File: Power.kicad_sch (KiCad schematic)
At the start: 15 parts, among them J5 Conn_01x02, U1 TPS62840YBGR, U13 TPS62840YBGR, U7 LTC2941IDCB-1#TRMPBF

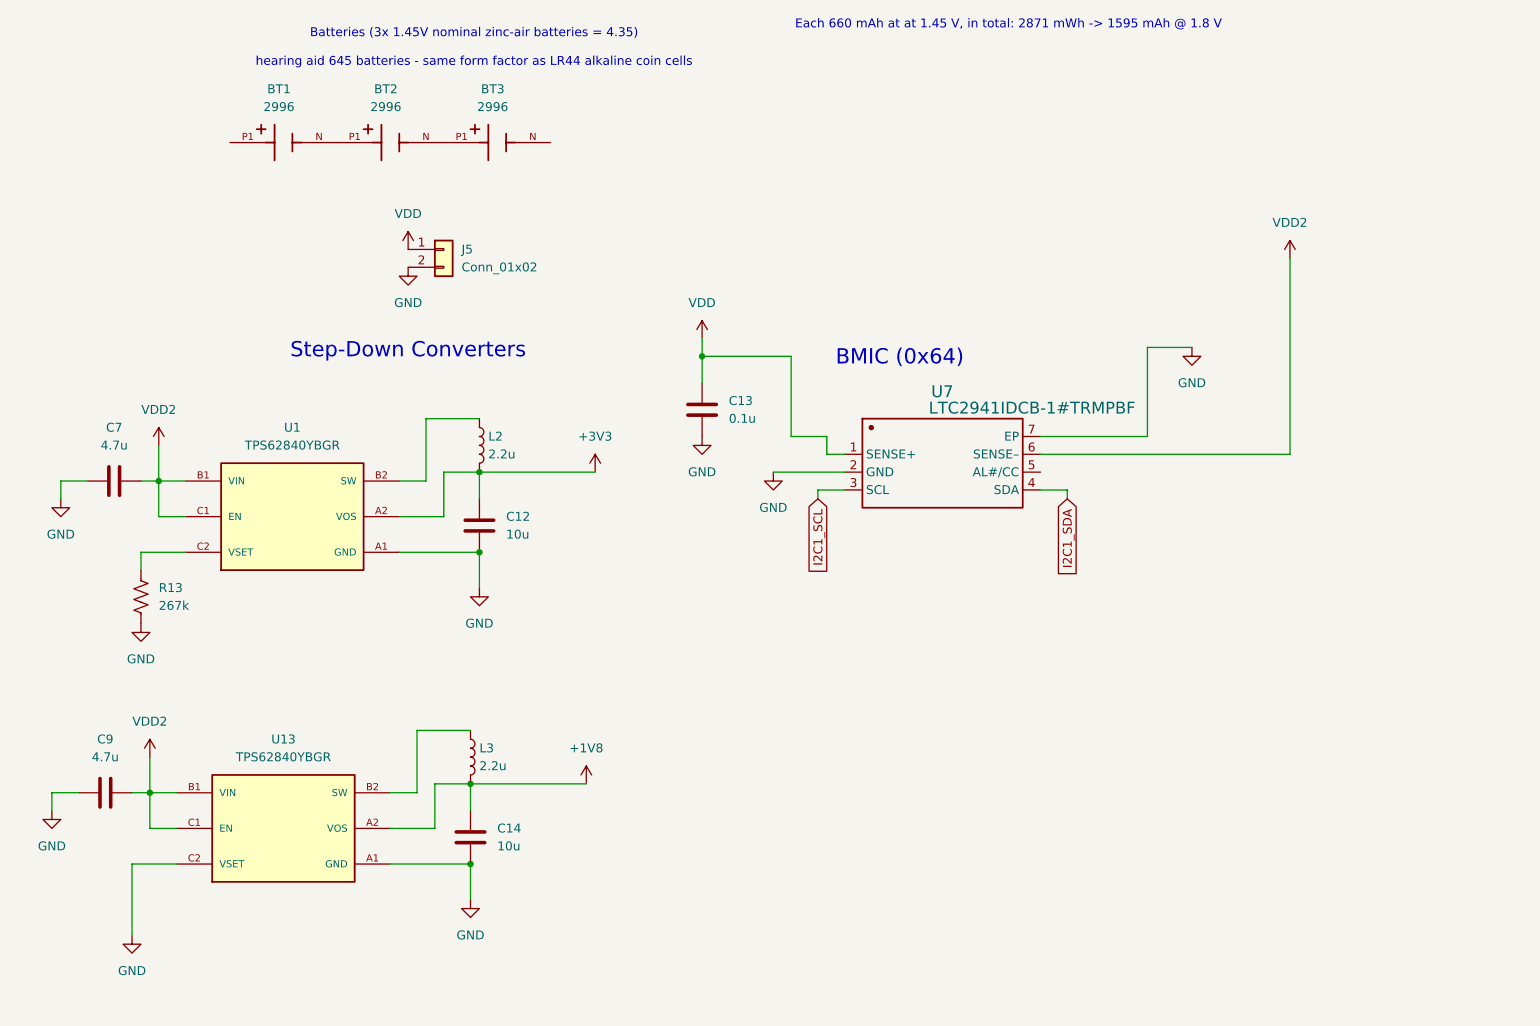
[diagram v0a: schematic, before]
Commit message: Add V2: STM32U575 LQFP-64 tag board and ST-Link dongle
The tag moves from the 23 × 18 mm STM32U585 WLCSP-90 layout to a
31.94 × 27.18 mm, 6-layer board (Pangotag_PCB_LCSC_compat4.kicad_pcb) with
an LQFP-64 STM32U575, a MAX-M10S GNSS module, a 32 GB eMMC and parts that
JLCPCB stocks. Adds the USB-C debug dongle, the intermediate revisions, the
JLCPCB production files, the project footprint and symbol libraries, BOMs
and renders, plus a README.

Stops tracking KiCad lock files, the local-history folder and .DS_Store,
and ignores them along with large 3D exports.
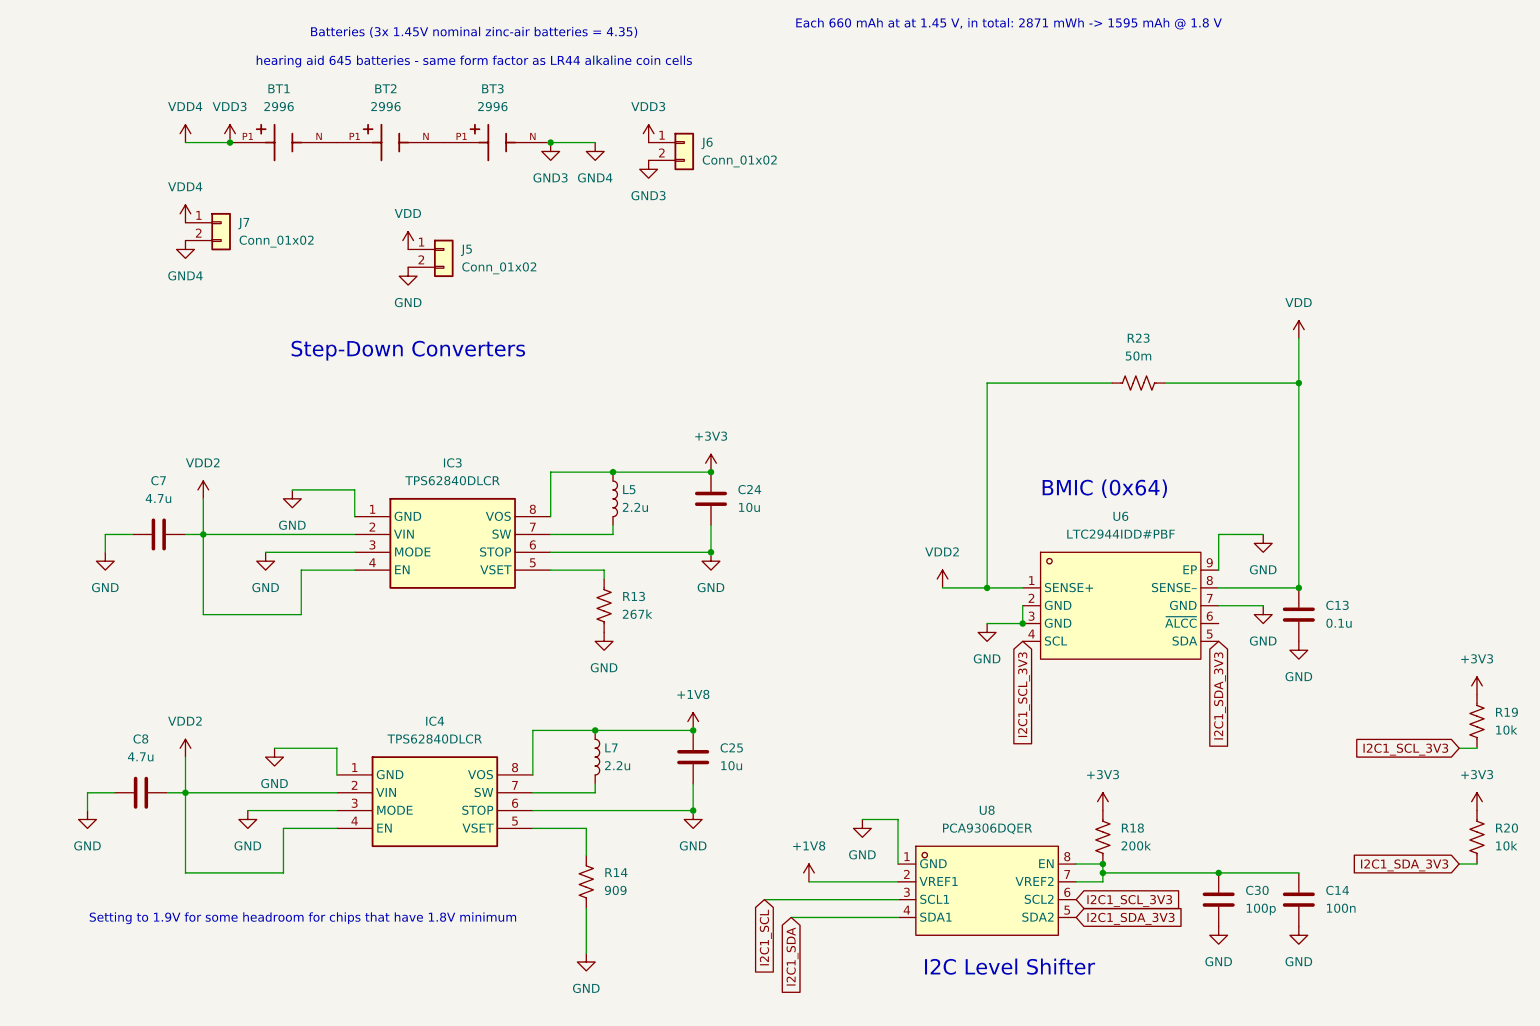
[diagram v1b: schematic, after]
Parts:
- removed C12: 10u, Capacitor_SMD:C_0201_0603Metric, symbol Device:C
- removed C9: 4.7u, Capacitor_SMD:C_0201_0603Metric, symbol Device:C
- removed L2, L3: 2.2u, Inductor_SMD:L_0201_0603Metric, symbol Device:L
- removed U1, U13: TPS62840YBGR, TPS62840YBGR:BGA6N40P3X2_146X96X50N, symbol TPS62840YBGR:TPS62840YBGR
- removed U7: LTC2941IDCB-1#TRMPBF, Package_DFN_QFN:DFN-6-1EP_3x2mm_P0.5mm_EP1.65x1.35mm, symbol LTC2941IDCB-1#TRMPBF
- added C24, C25: 10u, Capacitor_SMD:C_0402_1005Metric, symbol Device:C
- added C30: 100p, Capacitor_SMD:C_0201_0603Metric, symbol Device:C
- added C8: 4.7u, Capacitor_SMD:C_0201_0603Metric, symbol Device:C
- added IC3, IC4: TPS62840DLCR, SON50P150X200X100-8N-D, symbol TPS62840DLCR:TPS62840DLCR
- added J6, J7: Conn_01x02, Connector_Hirose:Hirose_DF57H-2P-1.2V_1x02_P1.2mm_Socket, symbol Connector_Generic:Conn_01x02
- added L5, L7: 2.2u, Inductor_SMD:L_0805_2012Metric, symbol Device:L
- added R14: 909, Resistor_SMD:R_0201_0603Metric, symbol Device:R_US
- added R18: 200k, Resistor_SMD:R_0201_0603Metric, symbol Device:R_US
- added R19, R20: 10k, Resistor_SMD:R_0201_0603Metric, symbol Device:R_US
- added R23: 50m, Resistor_SMD:R_0201_0603Metric, symbol Device:R_US
- added U6: LTC2944IDD#PBF, easyeda2kicad:DFN-8_L3.0-W3.0-P0.50-BL-EP, symbol easyeda2kicad:LTC2944IDD#PBF
- added U8: PCA9306DQER, easyeda2kicad:X2SON-8_L1.4-W1.0-P0.35-BL, symbol easyeda2kicad:PCA9306DQER
- C14: value 10u -> 100n
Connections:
- net +1V8: now also C25.1, IC4.8 (VOS), L7.1, U8.2 (VREF1); no longer C14.1
- net +3V3: now also C24.1, IC3.8 (VOS), L5.1, R18.1, R19.1, R20.1
- net GND: now also C24.2, C25.2, C30.2, C8.2, IC3.1 (GND), IC3.3 (MODE), IC3.6 (STOP), IC4.1 (GND), IC4.3 (MODE), IC4.6 (STOP), R14.2, U6.2 (GND), U6.3 (GND), U6.7 (GND), U6.9 (EP), U8.1 (GND)
- net I2C1_SCL: now also U8.3 (SCL1)
- net I2C1_SDA: now also U8.4 (SDA1)
- net VDD: now also R23.2, U6.8 (SENSE–)
- net VDD2: now also C8.1, IC3.2 (VIN), IC3.4 (EN), IC4.2 (VIN), IC4.4 (EN), R23.1, U6.1 (SENSE+)
- net VDD3: now reaches BT1.P1, BT1.P2
- net VDD3: now also J6.1 (Pin_1), J7.1 (Pin_1)
- net at R13.1: now also IC3.5 (VSET)
- net GND3: now reaches BT3.N
- net GND3: now also J6.2 (Pin_2), J7.2 (Pin_2)
- new net: C14.1, C30.1, R18.2, U8.7 (VREF2), U8.8 (EN)
- new net: IC4.5 (VSET), R14.1
- new net: IC3.7 (SW), L5.2
- new net: IC4.7 (SW), L7.2
- new net I2C1_SCL_3V3: R19.2, U6.4 (SCL), U8.6 (SCL2)
- new net I2C1_SDA_3V3: R20.2, U6.5 (SDA), U8.5 (SDA2)
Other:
- note added: "I2C Level Shifter"
- note added: "Setting to 1.9V for some headroom for chips that have 1.8V minimum"
- moved on the sheet: C13
